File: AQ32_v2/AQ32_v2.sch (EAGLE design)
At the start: 115 parts, among them Q2 BCV27, Q3 BCV27, Q5 BCV27, Q6 BCV27, U1 ITG-3200, U10 MS5611, U11 MIC5239, U13 74AHC1G86DCK, U2 STM32F10XVXT6, U3 74AHC1G86DCK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

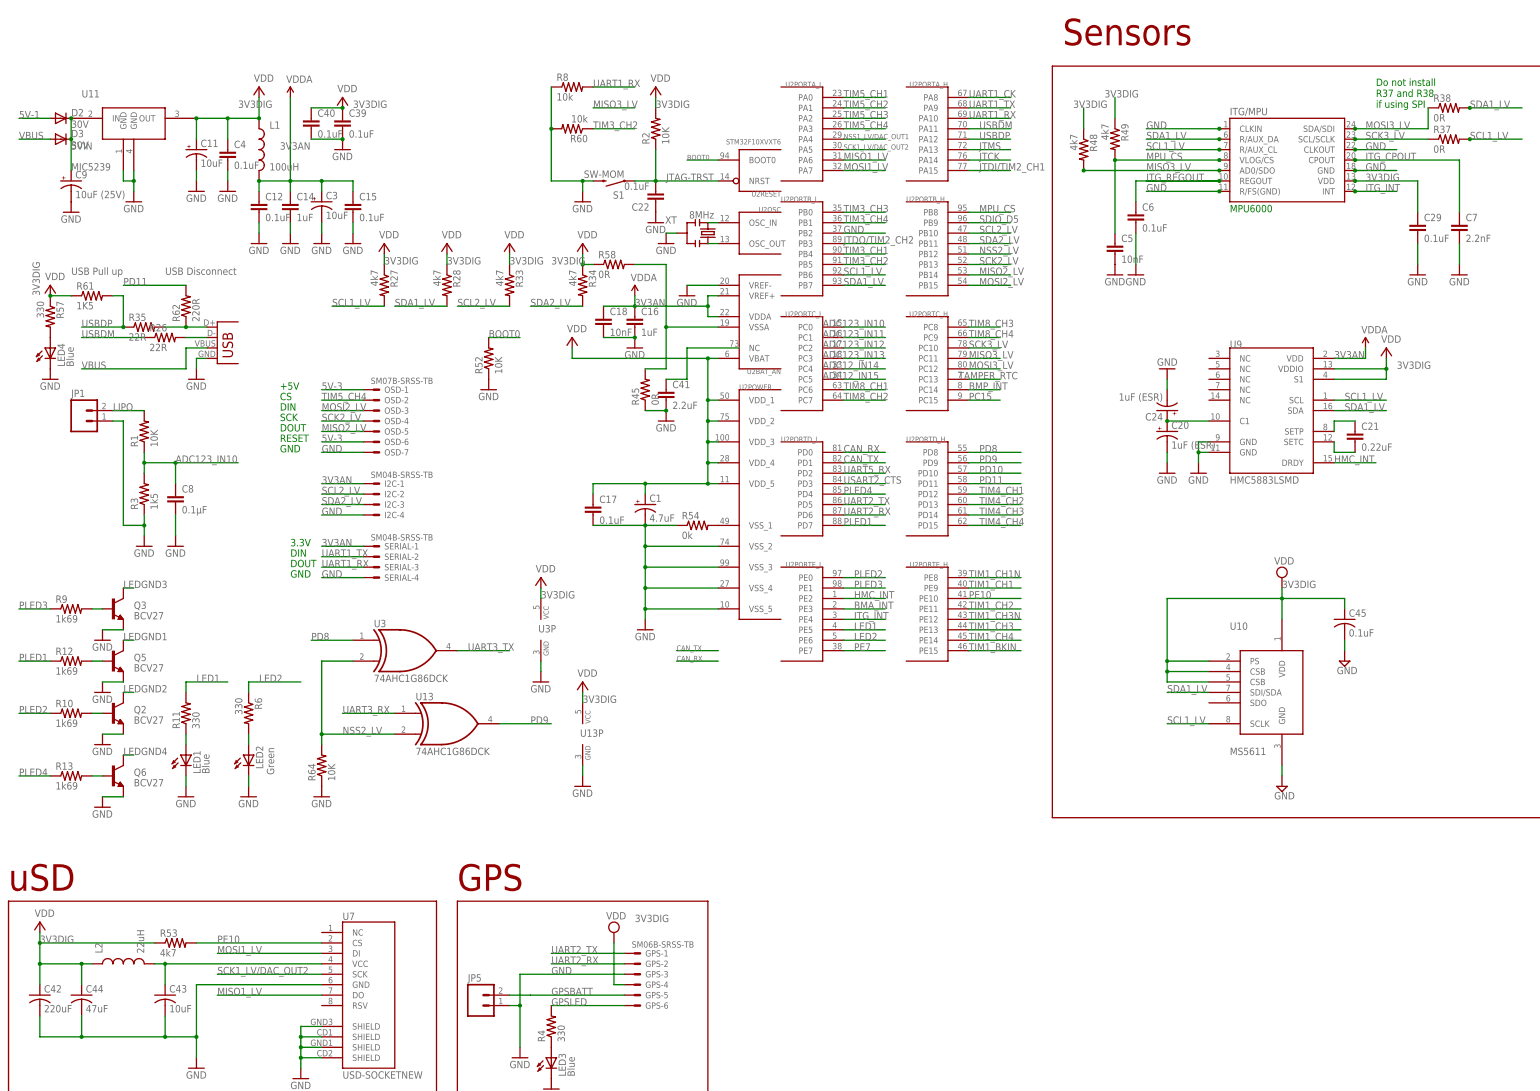
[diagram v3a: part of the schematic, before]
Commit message: moved vias away from under sensors, added more gnd vias, cleaned up BOM
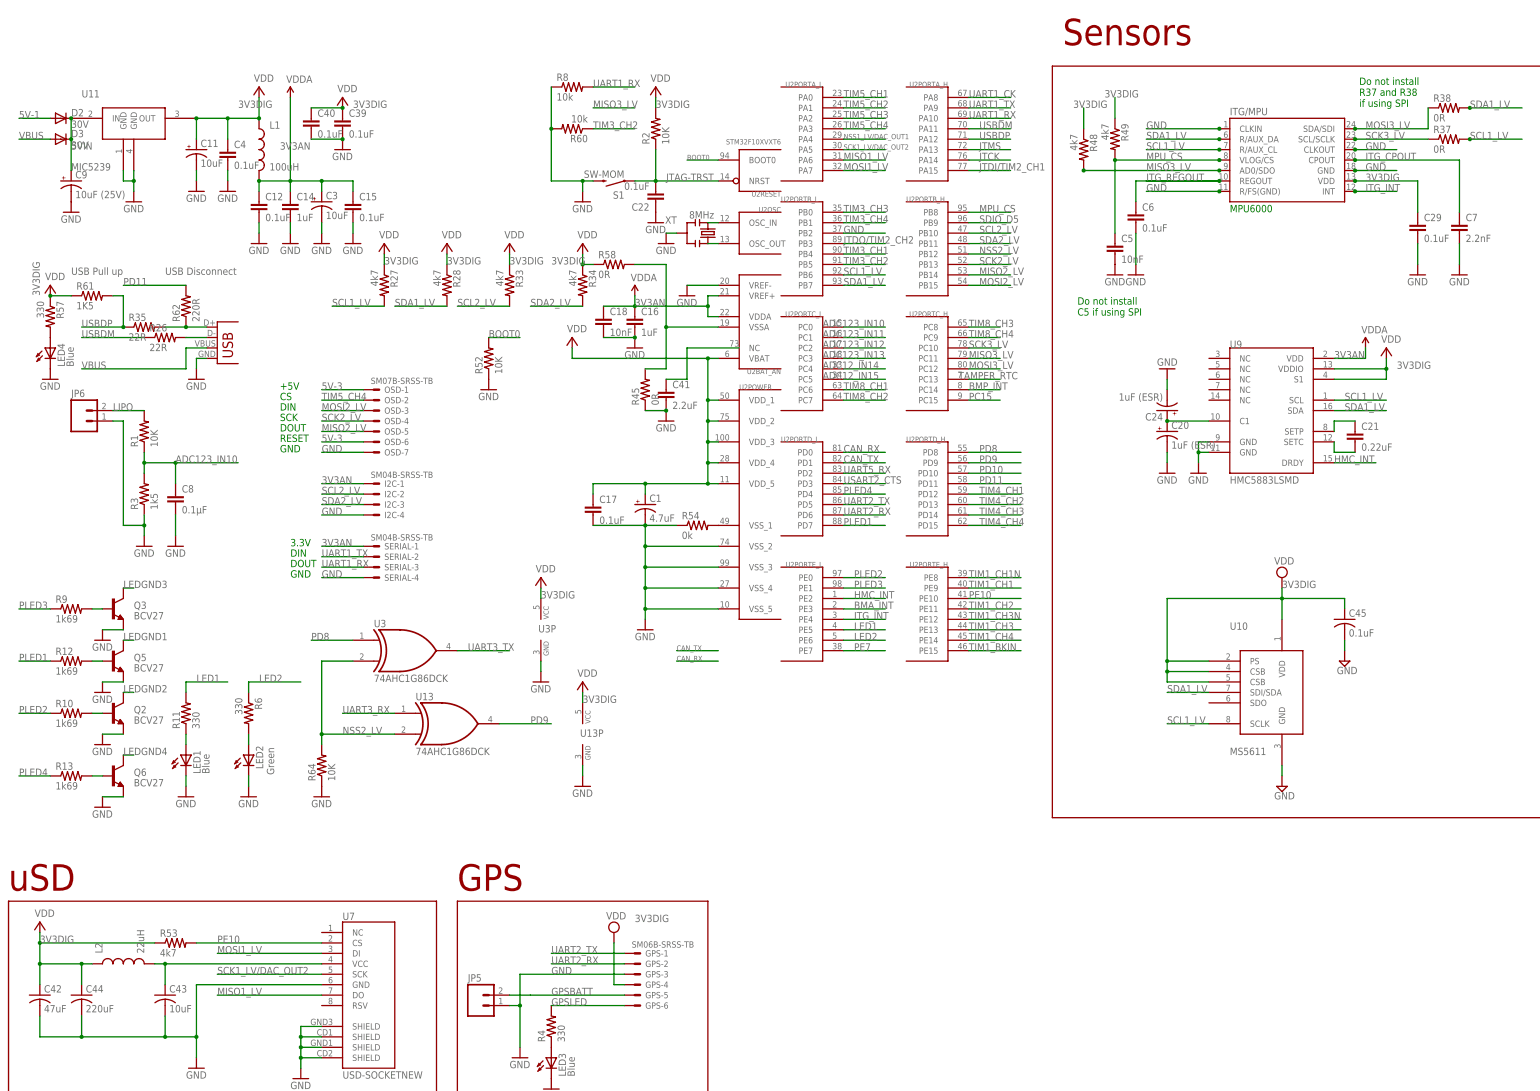
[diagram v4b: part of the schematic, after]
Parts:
- C42: value 220uF -> 47uF
- C44: value 47uF -> 220uF
- renumbered JP1 to JP6
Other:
- note added: "Do not install C5 if using SPI"
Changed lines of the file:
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@@
 <part name="R8" library="rcl" deviceset="R-US_" device="R0402" value="10k"/>
 <part name="R60" library="rcl" deviceset="R-US_" device="R0402" value="10k"/>
-<part name="C42" library="rcl" deviceset="C-US" device="C0805" value="220uF"/>
+<part name="C42" library="rcl" deviceset="C-US" device="C0805" value="47uF"/>
 <part name="C43" library="rcl" deviceset="C-US" device="C0805" value="10uF"/>
-<part name="C44" library="rcl" deviceset="C-US" device="C1206" value="47uF"/>
+<part name="C44" library="rcl" deviceset="C-US" device="C1206" value="220uF"/>
 <part name="U10" library="DSP-TI" deviceset="MS5611" device=""/>
 <part name="SUPPLY19" library="supply2" deviceset="GND" device=""/>
@@
 <part name="GND25" library="SparkFun" deviceset="GND" device=""/>
 <part name="SUPPLY2" library="supply2" deviceset="V+" device="" value="VDD"/>
-<part name="JP1" library="SparkFun-Connectors" deviceset="M02" device="PTH"/>
+<part name="JP6" library="SparkFun-Connectors" deviceset="M02" device="PTH"/>
 </parts>
 <sheets>
@@
 <text x="500.38" y="73.66" size="1.778" layer="91">AI4</text>
 <text x="500.38" y="76.2" size="1.778" layer="91">AI5</text>
-<text x="332.74" y="175.26" size="1.778" layer="91">Do not install
+<text x="328.676" y="175.514" size="1.778" layer="91">Do not install
 R37 and R38
 if using SPI</text>
+<text x="260.096" y="124.714" size="1.778" layer="91">Do not install
+C5 if using SPI</text>
 </plain>
 <instances>
@@
 <instance part="GND25" gate="1" x="129.54" y="35.56"/>
 <instance part="SUPPLY2" gate="1" x="129.54" y="60.96"/>
-<instance part="JP1" gate="G$1" x="17.78" y="99.06"/>
+<instance part="JP6" gate="G$1" x="17.78" y="99.06"/>
 </instances>
 <busses>
@@
 <pinref part="R3" gate="G$1" pin="1"/>
 <pinref part="GND15" gate="1" pin="GND"/>
-<pinref part="JP1" gate="G$1" pin="1"/>
+<pinref part="JP6" gate="G$1" pin="1"/>
 <wire x1="33.02" y1="73.66" x2="33.02" y2="71.12" width="0.1524" layer="91"/>
 <wire x1="25.4" y1="99.06" x2="27.94" y2="99.06" width="0.1524" layer="91"/>
@@
 <wire x1="33.02" y1="101.6" x2="25.4" y2="101.6" width="0.1524" layer="91"/>
 <label x="25.4" y="101.6" size="1.778" layer="95"/>
-<pinref part="JP1" gate="G$1" pin="2"/>
-</segment>
-</net>
+<pinref part="JP6" gate="G$1" pin="2"/>
+</segment>
+</net>

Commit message: moved BM closer to LED control, improved grounding for LED's
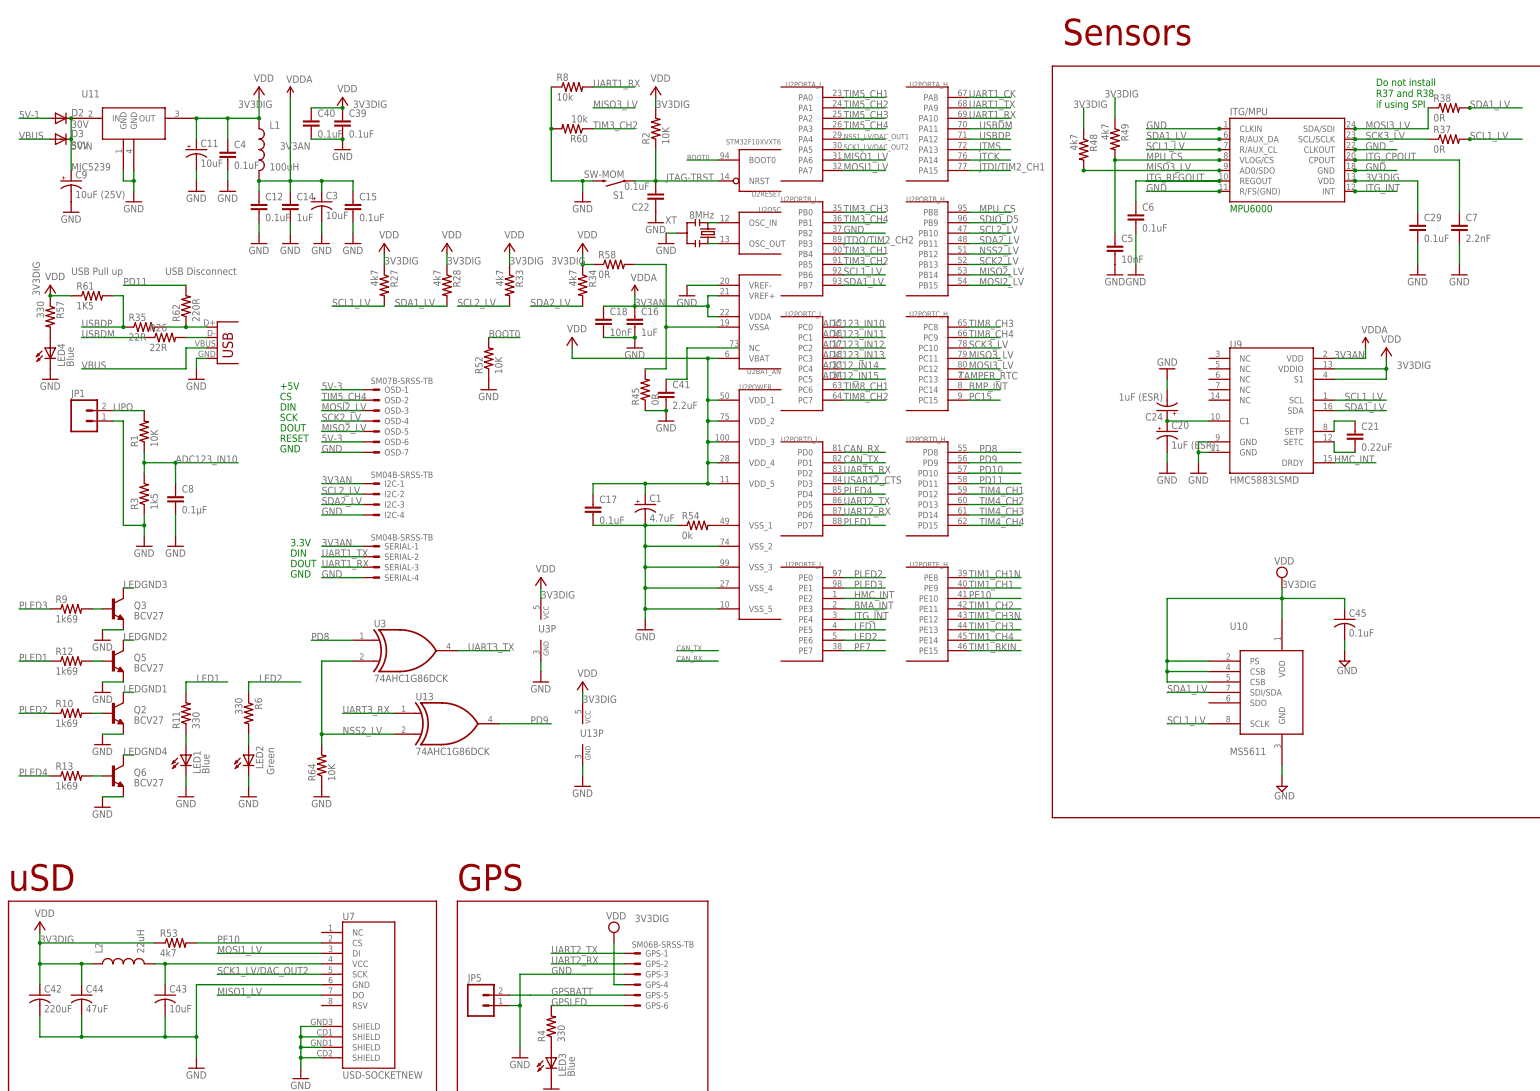
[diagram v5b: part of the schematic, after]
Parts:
- C42: value 47uF -> 220uF
- C44: value 220uF -> 47uF
- renumbered JP6 to JP1
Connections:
- net LEDGND1: now also Q2.C; no longer Q5.C
- net LEDGND2: now also Q5.C; no longer Q2.C
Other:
- note removed: "Do not install C5 if using SPI"
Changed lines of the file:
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@@
 <part name="R8" library="rcl" deviceset="R-US_" device="R0402" value="10k"/>
 <part name="R60" library="rcl" deviceset="R-US_" device="R0402" value="10k"/>
-<part name="C42" library="rcl" deviceset="C-US" device="C0805" value="47uF"/>
+<part name="C42" library="rcl" deviceset="C-US" device="C0805" value="220uF"/>
 <part name="C43" library="rcl" deviceset="C-US" device="C0805" value="10uF"/>
-<part name="C44" library="rcl" deviceset="C-US" device="C1206" value="220uF"/>
+<part name="C44" library="rcl" deviceset="C-US" device="C1206" value="47uF"/>
 <part name="U10" library="DSP-TI" deviceset="MS5611" device=""/>
 <part name="SUPPLY19" library="supply2" deviceset="GND" device=""/>
@@
 <part name="GND25" library="SparkFun" deviceset="GND" device=""/>
 <part name="SUPPLY2" library="supply2" deviceset="V+" device="" value="VDD"/>
-<part name="JP6" library="SparkFun-Connectors" deviceset="M02" device="PTH"/>
+<part name="JP1" library="SparkFun-Connectors" deviceset="M02" device="PTH"/>
 </parts>
 <sheets>
@@
 <text x="500.38" y="73.66" size="1.778" layer="91">AI4</text>
 <text x="500.38" y="76.2" size="1.778" layer="91">AI5</text>
-<text x="328.676" y="175.514" size="1.778" layer="91">Do not install
+<text x="332.74" y="175.26" size="1.778" layer="91">Do not install
 R37 and R38
 if using SPI</text>
-<text x="260.096" y="124.714" size="1.778" layer="91">Do not install
-C5 if using SPI</text>
 </plain>
 <instances>
@@
 <instance part="GND25" gate="1" x="129.54" y="35.56"/>
 <instance part="SUPPLY2" gate="1" x="129.54" y="60.96"/>
-<instance part="JP6" gate="G$1" x="17.78" y="99.06"/>
+<instance part="JP1" gate="G$1" x="17.78" y="99.06"/>
 </instances>
 <busses>
@@
 <pinref part="R3" gate="G$1" pin="1"/>
 <pinref part="GND15" gate="1" pin="GND"/>
-<pinref part="JP6" gate="G$1" pin="1"/>
+<pinref part="JP1" gate="G$1" pin="1"/>
 <wire x1="33.02" y1="73.66" x2="33.02" y2="71.12" width="0.1524" layer="91"/>
 <wire x1="25.4" y1="99.06" x2="27.94" y2="99.06" width="0.1524" layer="91"/>
@@
 <net name="LEDGND1" class="0">
 <segment>
+<pinref part="JP4-1" gate="G$1" pin="1"/>
+<wire x1="495.3" y1="25.4" x2="505.46" y2="25.4" width="0.1524" layer="91"/>
+<label x="495.3" y="25.4" size="1.778" layer="95"/>
+</segment>
+<segment>
+<wire x1="30.48" y1="33.02" x2="27.94" y2="33.02" width="0.1524" layer="91"/>
+<pinref part="Q2" gate="G$1" pin="C"/>
+<label x="27.94" y="33.02" size="1.778" layer="95"/>
+</segment>
+</net>
+<net name="LEDGND2" class="0">
+<segment>
+<pinref part="JP4-1" gate="G$1" pin="2"/>
+<wire x1="495.3" y1="27.94" x2="505.46" y2="27.94" width="0.1524" layer="91"/>
+<label x="495.3" y="27.94" size="1.778" layer="95"/>
+</segment>
+<segment>
 <wire x1="30.48" y1="45.72" x2="27.94" y2="45.72" width="0.1524" layer="91"/>
 <pinref part="Q5" gate="G$1" pin="C"/>
 <label x="27.94" y="45.72" size="1.778" layer="95"/>
-</segment>
-<segment>
-<pinref part="JP4-1" gate="G$1" pin="1"/>
-<wire x1="495.3" y1="25.4" x2="505.46" y2="25.4" width="0.1524" layer="91"/>
-<label x="495.3" y="25.4" size="1.778" layer="95"/>
-</segment>
-</net>
-<net name="LEDGND2" class="0">
-<segment>
-<wire x1="30.48" y1="33.02" x2="27.94" y2="33.02" width="0.1524" layer="91"/>
-<pinref part="Q2" gate="G$1" pin="C"/>
-<label x="27.94" y="33.02" size="1.778" layer="95"/>
-</segment>
-<segment>
-<pinref part="JP4-1" gate="G$1" pin="2"/>
-<wire x1="495.3" y1="27.94" x2="505.46" y2="27.94" width="0.1524" layer="91"/>
-<label x="495.3" y="27.94" size="1.778" layer="95"/>
 </segment>
 </net>
@@
 <wire x1="33.02" y1="101.6" x2="25.4" y2="101.6" width="0.1524" layer="91"/>
 <label x="25.4" y="101.6" size="1.778" layer="95"/>
-<pinref part="JP6" gate="G$1" pin="2"/>
-</segment>
-</net>
+<pinref part="JP1" gate="G$1" pin="2"/>
+</segment>
+</net>
